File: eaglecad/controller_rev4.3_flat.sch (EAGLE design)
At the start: 79 parts, among them U100 STM32L452XX_QFPN48, U101 TCAN330, U200 TPS63070, U300 STSPIN230, U301 TSV991ILT, U302 AS5047P, U400 STSPIN250, U401 TSV991ILT, X101 ABM10-16MHz

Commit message: board flattening
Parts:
- added TP1, TP10, TP11, TP12, TP13, TP14, TP15, TP16, TP17, TP18, TP19, TP2, TP20, TP21, TP22, TP23, TP24, TP25, TP26, TP27, TP28, TP29, TP3, TP30, TP31, TP4, TP5, TP6, TP7, TP8, TP9: TEST-POINT-LARGE, oresat-misc:TEST-POINT-LARGE
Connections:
- net 3.3V: now also TP29.TP, TP30.TP, TP31.TP
- net ADDR_0: now also TP14.TP
- net ADDR_1: now also TP15.TP
- net BLDC_CURR_FDB: now also TP2.TP
- net BLDC_EN: now also TP11.TP
- net BLDC_FAULT: now also TP10.TP
- net BLDC_INUH: now also TP23.TP
- net BLDC_INUL: now also TP7.TP
- net BLDC_INVH: now also TP24.TP
- net BLDC_INVL: now also TP8.TP
- net BLDC_INWH: now also TP25.TP
- net BLDC_INWL: now also TP9.TP
- net BLDC_STBY: now also TP22.TP
- net CAN_RX: now also TP27.TP
- net CAN_SILENT: now also TP28.TP
- net CAN_TX: now also TP26.TP
- net DEBUG_1: now also TP13.TP
- net DEBUG_2: now also TP6.TP
- net I2C_SCL: now also TP20.TP
- net I2C_SDA: now also TP21.TP
- net MAG_CURR_FDB: now also TP1.TP
- net MAG_DIR: now also TP16.TP
- net MAG_EN: now also TP19.TP
- net MAG_FAULT: now also TP18.TP
- net MAG_PWM: now also TP12.TP
- net MAG_STBY: now also TP17.TP
- net SPI1_CS: now also TP3.TP
- net SPI1_MISO: now also TP5.TP
- net SPI1_SCK: now also TP4.TP
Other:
- moved on the sheet: R102, R103

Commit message: Flattening the board
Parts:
- removed C501: DEBUG_CON, oresat-ACS_driver_board:DEBUG_CON
- added DEBUG1: (no value), pinhead:PINHD-1X2
- added J1: (no value), SparkFun-Connectors:6_PIN_SERIAL_TARGETSILK
- added LED5, LED6: BLUE, led:LEDCHIPLED_0603
- added LED7: AMBER, led:LEDCHIPLED_0603
- added LED8: GREEN, led:LEDCHIPLED_0603
- added R5, R6: 100, oresat-rcl:R-US_0402-B-NOSILK
- added R7: 1.3k, oresat-rcl:R-US_0402-B-NOSILK
- added R8: 330, oresat-rcl:R-US_0402-B-NOSILK
- added SWD1: 1.27MM-SWD-CONNECTOR, J-CNC-3220-10-0100-00-ARM-SWD-port:1.27MM-SWD-CONNECTOR
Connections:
- new net N$5: LED5.C, R5.2
- new net N$6: LED6.C, R6.2
- new net N$7: LED7.C, R7.2
- new net N$8: LED8.C, R8.2
- net 3.3V: now also LED8.A, SWD1.VTREF; no longer C501.2
- net DEBUG_1: now also DEBUG1.1, LED6.A; no longer C501.3
- net DEBUG_2: now also DEBUG1.2, LED5.A; no longer C501.4
- net GND: now also J1.GND, R5.1, R6.1, R7.1, R8.1, SWD1.GND, SWD1.GND@2; no longer C501.10
- net NRST: now also SWD1.!RESET; no longer C501.7
- net SWCLK: now also SWD1.SWDCLK/TCK; no longer C501.9
- net SWDIO: now also SWD1.SWDIO/TMS; no longer C501.8
- net UART_RX: now also J1.RXI; no longer C501.5
- net UART_TX: now also J1.TXO; no longer C501.6
- net VBUS: now also J1.VCC, LED7.A; no longer C501.1
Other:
- note removed: "CON501"
- note removed: "CONNECTION TO ACS DRIVER PROG. ADDAPTER"
- note removed: "DEBUG CONN"
- moved on the sheet: R101

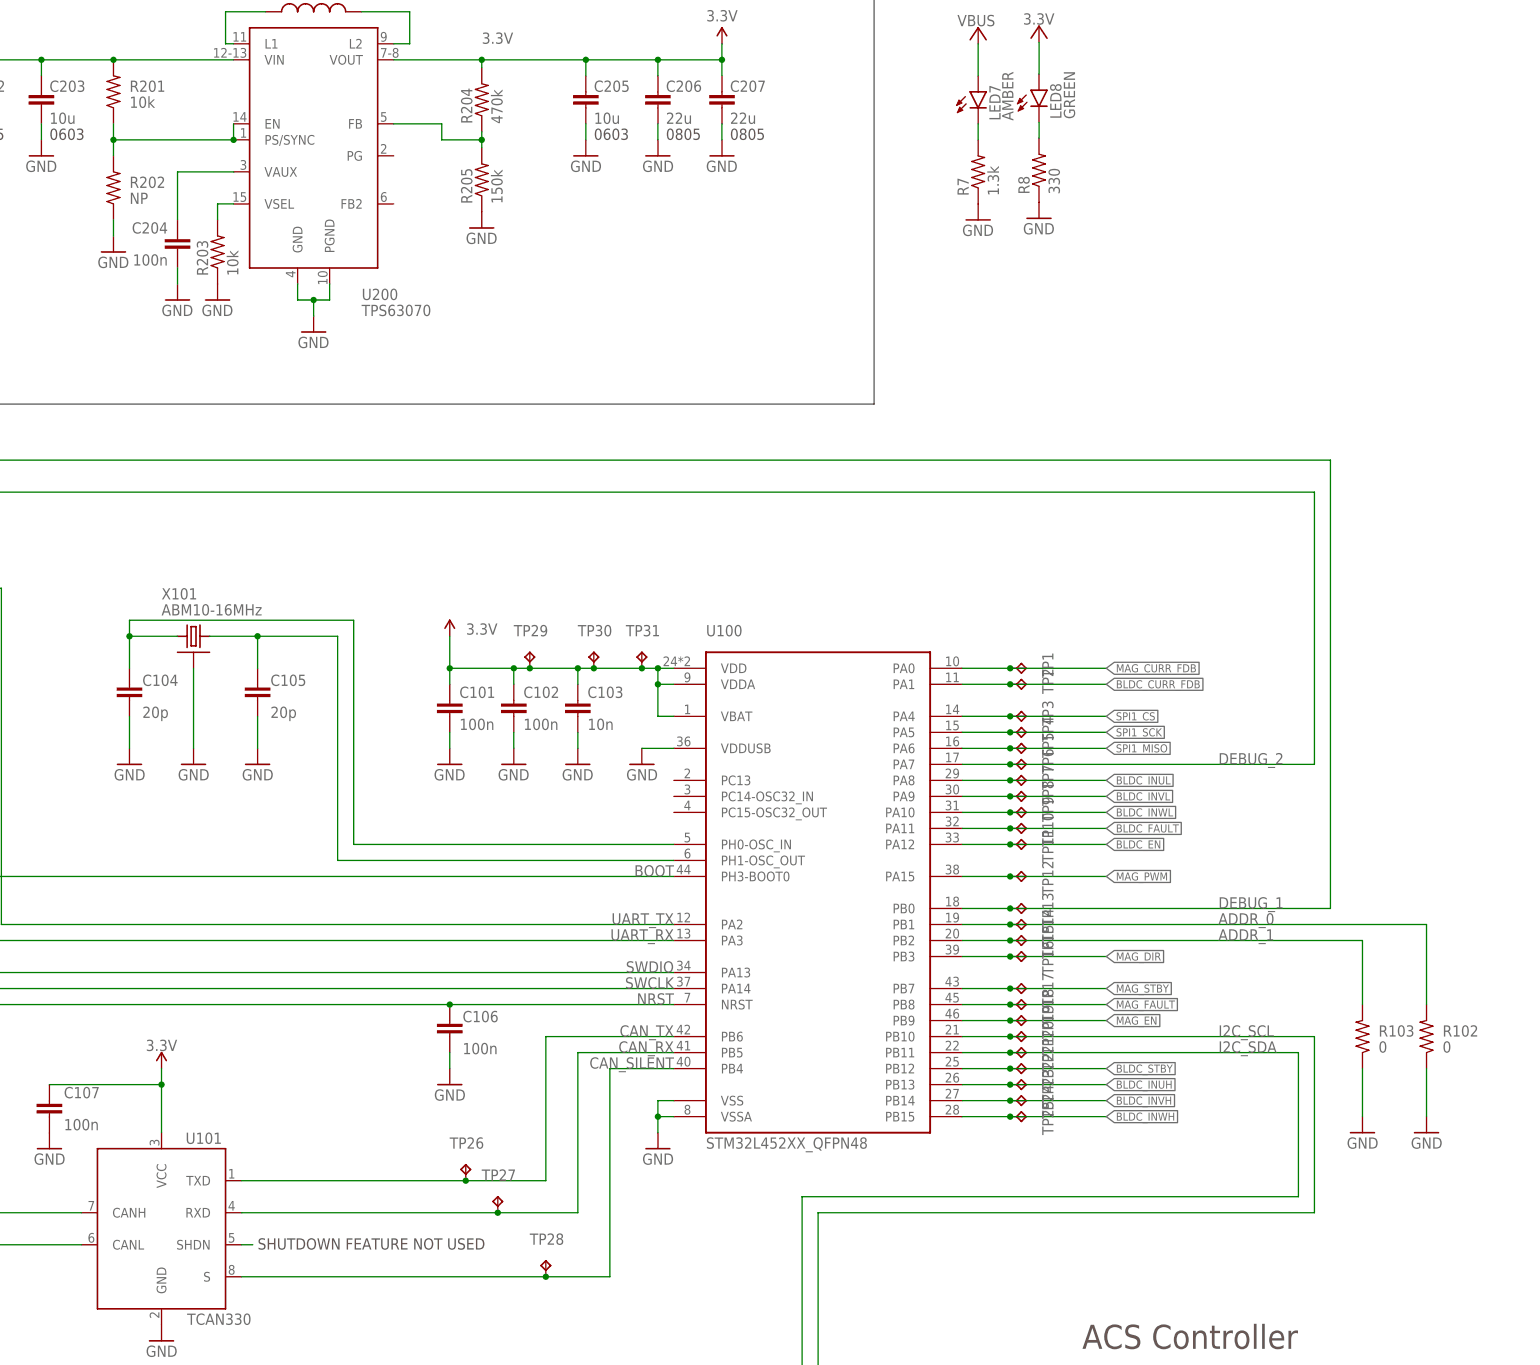
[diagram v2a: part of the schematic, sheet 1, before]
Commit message: Flattening rev 4.3
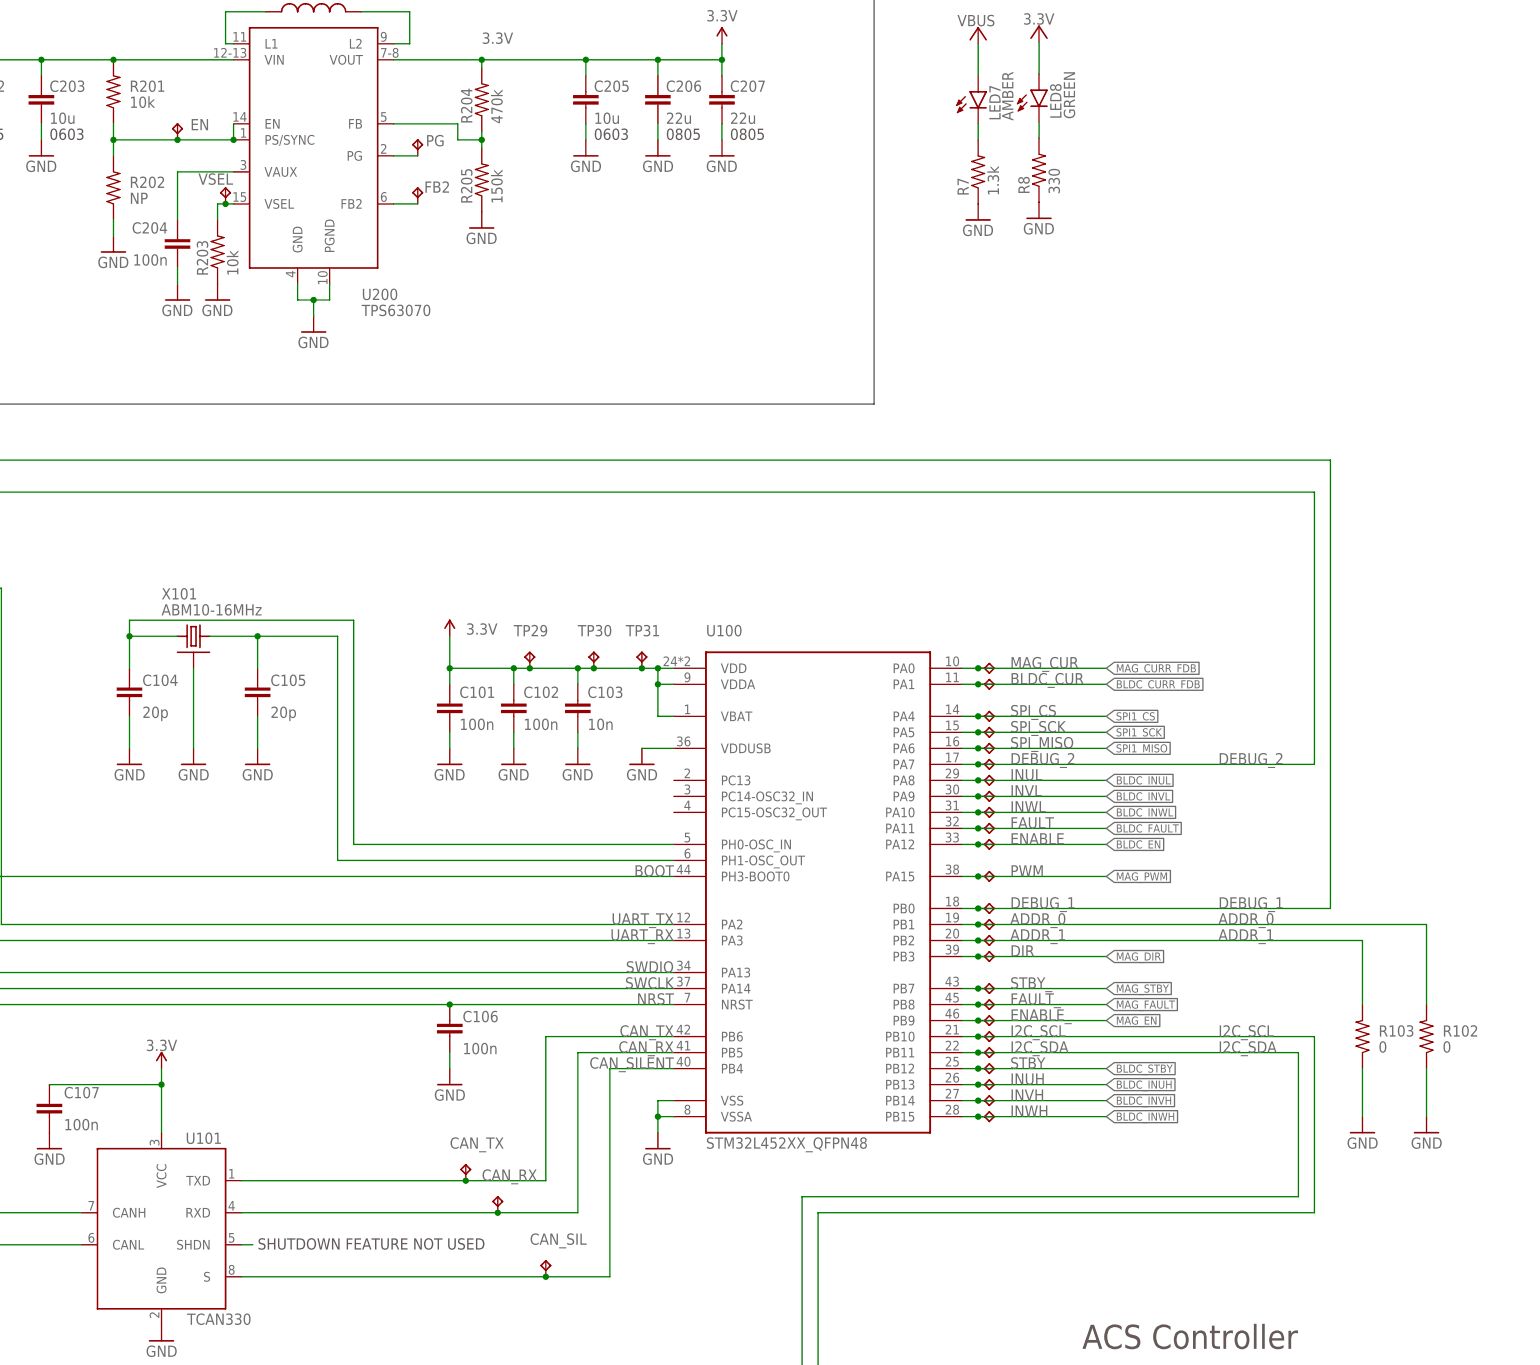
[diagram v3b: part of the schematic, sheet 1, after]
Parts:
- removed TP1, TP10, TP11, TP12, TP13, TP14, TP15, TP16, TP17, TP18, TP19, TP2, TP20, TP21, TP22, TP23, TP24, TP25, TP3, TP4, TP5, TP6, TP7, TP8, TP9: TEST-POINT-LARGE, oresat-misc:TEST-POINT-LARGE
- added ADDR_0, ADDR_1, BLDC_CUR, DEBUG_1, DEBUG_2, DIR, EN, ENABLE, ENABLE_, FAULT, FAULT_, FB2, I2C_SCL, I2C_SDA, INUH, INUL, INVH, INVL, INWH, INWL, MAG_CUR, PG, PWM, SPI_CS, SPI_MISO, SPI_SCK, STBY, STBY_, VSEL: TEST-POINT-LARGE, oresat-misc:TEST-POINT-LARGE
- renumbered TP26 to CAN_TX, TP27 to CAN_RX, TP28 to CAN_SIL
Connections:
- new net FB2: FB2.TP, U200.FB2
- new net PG: PG.TP, U200.PG
- net ADDR_0: now also ADDR_0.TP; no longer TP14.TP
- net ADDR_1: now also ADDR_1.TP; no longer TP15.TP
- net BLDC_CURR_FDB: now also BLDC_CUR.TP; no longer TP2.TP
- net BLDC_EN: now also ENABLE.TP; no longer TP11.TP
- net BLDC_FAULT: now also FAULT.TP; no longer TP10.TP
- net BLDC_INUH: now also INUH.TP; no longer TP23.TP
- net BLDC_INUL: now also INUL.TP; no longer TP7.TP
- net BLDC_INVH: now also INVH.TP; no longer TP24.TP
- net BLDC_INVL: now also INVL.TP; no longer TP8.TP
- net BLDC_INWH: now also INWH.TP; no longer TP25.TP
- net BLDC_INWL: now also INWL.TP; no longer TP9.TP
- net BLDC_STBY: now also STBY.TP; no longer TP22.TP
- net DEBUG_1: now also DEBUG_1.TP; no longer TP13.TP
- net DEBUG_2: now also DEBUG_2.TP; no longer TP6.TP
- net I2C_SCL: now also I2C_SCL.TP; no longer TP20.TP
- net I2C_SDA: now also I2C_SDA.TP; no longer TP21.TP
- net MAG_CURR_FDB: now also MAG_CUR.TP; no longer TP1.TP
- net MAG_DIR: now also DIR.TP; no longer TP16.TP
- net MAG_EN: now also ENABLE_.TP; no longer TP19.TP
- net MAG_FAULT: now also FAULT_.TP; no longer TP18.TP
- net MAG_PWM: now also PWM.TP; no longer TP12.TP
- net MAG_STBY: now also STBY_.TP; no longer TP17.TP
- net SPI1_CS: now also SPI_CS.TP; no longer TP3.TP
- net SPI1_MISO: now also SPI_MISO.TP; no longer TP5.TP
- net SPI1_SCK: now also SPI_SCK.TP; no longer TP4.TP
- net TPS-EN2: now also EN.TP
- net TPS-VSEL2: now also VSEL.TP

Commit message: traces routed, still needs polygons and planes
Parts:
- removed DEBUG1: (no value), pinhead:PINHD-1X2
- removed R102, R103: 0, rcl_custom:R-US_0402-B-NOSILK
- removed R7: 1.3k, oresat-rcl:R-US_0402-B-NOSILK
- removed R8: 330, oresat-rcl:R-US_0402-B-NOSILK
- added J2: J-SAMTEC-TFM-120-X1-XXX-D-RA, J-Samtec-TFM-120-X1-XXX-D-RA:J-SAMTEC-TFM-120-X1-XXX-D-RA
- added JP1: (no value), pinhead:PINHD-1X4
- added JP2: (no value), pinhead:PINHD-2X4
- added JP3: (no value), pinhead:PINHD-1X9
- added LED1, LED2: BLUE, led:LEDCHIPLED_0603
- added R1: 1.3k, oresat-rcl:R-US_0402-B-NOSILK
- added R2: 330, oresat-rcl:R-US_0402-B-NOSILK
- added R3, R4: 100, oresat-rcl:R-US_0402-B-NOSILK
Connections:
- new net DEBUG_3: JP1.3, JP2.1, LED1.A
- new net DEBUG_4: JP1.4, JP2.5, LED2.A
- new net N$1: LED1.C, R5.2
- new net N$2: LED2.C, R6.2
- new net V_BATT: J2.21, J2.22, J2.23, J2.24, J2.25, J2.26
- net ADDR_0: now also JP2.2, JP2.4; no longer R102.2
- net ADDR_1: now also JP2.6, JP2.8; no longer R103.2
- net BOOT: now also JP3.6
- net CAN_H: now also J2.17, J2.18, JP3.3
- net CAN_L: now also J2.19, J2.20, JP3.2
- net DEBUG_1: now also JP1.1, U100.PA7; no longer DEBUG1.1, U100.PB0
- net DEBUG_2: now also JP1.2, U100.PB0; no longer DEBUG1.2, U100.PA7
- net GND: now also J2.27, J2.28, J2.29, J2.30, J2.31, J2.32, J2.37, J2.38, JP2.3, JP2.7, JP3.9, R1.1, R2.1, R3.1, R4.1; no longer R102.1, R103.1, R7.1, R8.1
- net I2C_SCL: now also JP3.4
- net I2C_SDA: now also JP3.5
- net N$5: now also R4.2; no longer R5.2
- net N$6: now also R3.2; no longer R6.2
- net N$7: now also R1.2; no longer R7.2
- net N$8: now also R2.2; no longer R8.2
- net OUT1: now also JP3.7
- net OUT2: now also JP3.8
- net VBUS: now also JP3.1
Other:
- note added: "Main OreSat Card Connector"
- moved on the sheet: C101, C102, C103, DEBUG_1, DEBUG_2, J1, LED5, LED6, LED7, LED8, R101, R5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

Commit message: Board Flattened ready for review
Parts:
- removed JP301: (no value), pinhead-2:PINHD-1X03_2.00
- removed LED7: AMBER, led:LEDCHIPLED_0603
- removed LED8: GREEN, led:LEDCHIPLED_0603
- added J301, J302: (no value), pinhead:PINHD-2X3
- added LED3, LED4: BLUE, led:LEDCHIPLED_0603
- added LED301: CLX6E-FKC, D-Cree-CLX6E-RGB-LED:CLX6E-FKC
- added R7: 380, rcl_custom:R-US_0402-B-NOSILK
- added R8: 400, rcl_custom:R-US_0402-B-NOSILK
- added R9: 320, rcl_custom:R-US_0402-B-NOSILK
- LED1: value BLUE -> AMBER
- LED2: value BLUE -> GREEN
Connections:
- removed net V_BATT: J2.21, J2.22, J2.23, J2.24, J2.25, J2.26
- new net N$10: J301.1, J301.2
- new net N$11: J302.2, LED301.BA
- new net N$12: J302.4, LED301.GA
- new net N$13: J302.6, LED301.RA
- new net N$14: LED301.BC, R7.2
- new net N$15: LED301.GC, R8.2
- new net N$16: LED301.RC, R9.2
- new net N$4: J301.5, J301.6
- new net N$9: J301.3, J301.4
- net 3.3V: now also LED2.A; no longer LED8.A
- net DEBUG_1: now also LED3.A; no longer LED6.A
- net DEBUG_2: now also LED4.A; no longer LED5.A
- net DEBUG_3: now also LED5.A; no longer LED1.A
- net DEBUG_4: now also LED6.A; no longer LED2.A
- net GND: now also R7.1, R8.1, R9.1
- net N$1: now also LED5.C; no longer LED1.C
- net N$2: now also LED6.C; no longer LED2.C
- net N$5: now also LED4.C; no longer LED5.C
- net N$6: now also LED3.C; no longer LED6.C
- net N$7: now also LED1.C; no longer LED7.C
- net N$8: now also LED2.C; no longer LED8.C
- net U: now also J302.1; no longer JP301.1
- net V: now also J302.3; no longer JP301.2
- net VBUS: now also J2.21, J2.22, J2.23, J2.24, J2.25, J2.26, LED1.A; no longer LED7.A
- net W: now also J302.5; no longer JP301.3
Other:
- moved on the sheet: C306, C307, C308, C309, LED1, LED2, LED5, LED6, R303, R304, R305, R306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

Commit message: Flat ready for review for real this time
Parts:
- renumbered TP29 to 3.3V_A, TP30 to 3.3V_B, TP31 to 3.3V_C
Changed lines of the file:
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@@
 <part name="CAN_SIL" library="oresat-misc" deviceset="TEST-POINT-LARGE" device=""/>
 <part name="CAN_RX" library="oresat-misc" deviceset="TEST-POINT-LARGE" device=""/>
-<part name="TP29" library="oresat-misc" deviceset="TEST-POINT-LARGE" device=""/>
-<part name="TP30" library="oresat-misc" deviceset="TEST-POINT-LARGE" device=""/>
-<part name="TP31" library="oresat-misc" deviceset="TEST-POINT-LARGE" device=""/>
+<part name="3.3V_C" library="oresat-misc" deviceset="TEST-POINT-LARGE" device=""/>
+<part name="3.3V_A" library="oresat-misc" deviceset="TEST-POINT-LARGE" device=""/>
+<part name="3.3V_B" library="oresat-misc" deviceset="TEST-POINT-LARGE" device=""/>
 <part name="SWD1" library="J-CNC-3220-10-0100-00-ARM-SWD-port" deviceset="1.27MM-SWD-CONNECTOR" device=""/>
 <part name="J1" library="SparkFun-Connectors" library_urn="urn:adsk.eagle:library:513" deviceset="6_PIN_SERIAL_TARGET" device="SILK" package3d_urn="urn:adsk.eagle:package:37995/1"/>
@@
 <attribute name="NAME" x="246.38" y="53.34" size="1.778" layer="95"/>
 </instance>
-<instance part="TP29" gate="G$1" x="251.46" y="137.16" smashed="yes">
-<attribute name="NAME" x="248.92" y="139.7" size="1.778" layer="95"/>
-</instance>
-<instance part="TP30" gate="G$1" x="261.62" y="137.16" smashed="yes">
-<attribute name="NAME" x="259.08" y="139.7" size="1.778" layer="95"/>
-</instance>
-<instance part="TP31" gate="G$1" x="271.78" y="137.16" smashed="yes">
-<attribute name="NAME" x="269.24" y="139.7" size="1.778" layer="95"/>
+<instance part="3.3V_C" gate="G$1" x="271.78" y="137.16" smashed="yes">
+<attribute name="NAME" x="271.78" y="139.7" size="1.778" layer="95" rot="R90"/>
+</instance>
+<instance part="3.3V_A" gate="G$1" x="251.46" y="137.16" smashed="yes">
+<attribute name="NAME" x="251.46" y="139.7" size="1.778" layer="95" rot="R90"/>
+</instance>
+<instance part="3.3V_B" gate="G$1" x="261.62" y="137.16" smashed="yes">
+<attribute name="NAME" x="261.62" y="139.7" size="1.778" layer="95" rot="R90"/>
 </instance>
 <instance part="SWD1" gate="J" x="119.38" y="83.82" smashed="yes" rot="MR0">
@@
 <wire x1="274.32" y1="127" x2="274.32" y2="132.08" width="0.1524" layer="91"/>
 <junction x="274.32" y="132.08"/>
-<wire x1="274.32" y1="134.62" x2="271.78" y2="134.62" width="0.1524" layer="91"/>
+<wire x1="274.32" y1="134.62" x2="261.62" y2="134.62" width="0.1524" layer="91"/>
 <pinref part="SUPPLY6" gate="G$1" pin="3.3V"/>
-<wire x1="271.78" y1="134.62" x2="261.62" y2="134.62" width="0.1524" layer="91"/>
-<wire x1="261.62" y1="134.62" x2="259.08" y2="134.62" width="0.1524" layer="91"/>
-<wire x1="259.08" y1="134.62" x2="251.46" y2="134.62" width="0.1524" layer="91"/>
-<wire x1="251.46" y1="134.62" x2="248.92" y2="134.62" width="0.1524" layer="91"/>
+<wire x1="261.62" y1="134.62" x2="251.46" y2="134.62" width="0.1524" layer="91"/>
+<wire x1="251.46" y1="134.62" x2="259.08" y2="134.62" width="0.1524" layer="91"/>
+<wire x1="259.08" y1="134.62" x2="271.78" y2="134.62" width="0.1524" layer="91"/>
+<wire x1="271.78" y1="134.62" x2="248.92" y2="134.62" width="0.1524" layer="91"/>
 <wire x1="248.92" y1="134.62" x2="238.76" y2="134.62" width="0.1524" layer="91"/>
 <wire x1="238.76" y1="139.7" x2="238.76" y2="134.62" width="0.1524" layer="91"/>
@@
 <wire x1="259.08" y1="132.08" x2="259.08" y2="134.62" width="0.1524" layer="91"/>
 <junction x="259.08" y="134.62"/>
-<pinref part="TP29" gate="G$1" pin="TP"/>
+<pinref part="3.3V_C" gate="G$1" pin="TP"/>
+<junction x="271.78" y="134.62"/>
+<pinref part="3.3V_A" gate="G$1" pin="TP"/>
 <junction x="251.46" y="134.62"/>
-<pinref part="TP30" gate="G$1" pin="TP"/>
+<pinref part="3.3V_B" gate="G$1" pin="TP"/>
 <junction x="261.62" y="134.62"/>
-<pinref part="TP31" gate="G$1" pin="TP"/>
-<junction x="271.78" y="134.62"/>
-</segment>
-<segment>
+</segment>
+<segment>
